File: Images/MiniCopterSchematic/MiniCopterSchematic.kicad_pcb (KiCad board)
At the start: 2 copper layers, 78.6 x 58.6 mm, 42 parts, among them J1 MPU6050, M1 Motor_DC_1, M2 Motor_DC_2, M3 Motor_DC_3, M4 Motor_DC_4, Q1 FQP20NO6L, Q2 FQP20NO6L, Q3 FQP20NO6L, Q4 FQP20NO6L

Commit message: Working on routing
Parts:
- moved Q3 13.1 mm to (92.0, 113.6)
- moved Q1 12.7 mm to (79.4, 119.0)
- moved Q4 6.32 mm to (79.3, 113.6)
- moved Q2 0.99 mm to (92.0, 119.0)
- moved kibuzzard-6440EF4B 0.98 mm to (81.6, 110.2)
- moved kibuzzard-6440D5EF 0.64 mm to (97.5, 110.6)
- moved kibuzzard-6440D61E 0.64 mm to (94.5, 109.6)
- moved kibuzzard-6440D635 0.64 mm to (91.5, 109.6)
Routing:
- net +BATT: track 0.00 -> 155.6 mm
- net Net-(Q2-Pad1): track 0.00 -> 68.1 mm
- net MOTOR_1: track 5.52 -> 56.7 mm, vias 0 -> 6
- net Net-(Q3-Pad1): track 0.00 -> 48.5 mm
- net +3V3: track 0.00 -> 29.6 mm, vias 0 -> 2
- net MOTOR_4: track 4.33 -> 30.7 mm
- net Net-(M1-Pad2): track 0.00 -> 23.9 mm
- net MOTOR_2: track 4.30 -> 24.1 mm, vias 0 -> 2
- net MOTOR_3: track 7.87 -> 21.4 mm
- net Net-(Q4-Pad1): track 0.00 -> 9.59 mm
- net SDA: track 30.3 -> 29.6 mm

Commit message: Working on PCB
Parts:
- added kibuzzard-64457E06: G***, kibuzzard-64457E06, F.Cu at (92.0, 127.0)
- added kibuzzard-64457F3E: G***, kibuzzard-64457F3E, B.Cu at (131.0, 95.0)
- moved M4 4.00 mm to (78.0, 97.0)
- moved kibuzzard-6440B803 4.00 mm to (78.0, 104.0)
- moved kibuzzard-6440B80B 4.00 mm to (78.0, 90.0)
- moved M3 1.00 mm to (101.0, 80.0)
- moved kibuzzard-6440EF4B 0.50 mm to (81.6, 110.7)
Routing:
- net Net-(M4-Pad2): track 9.59 -> 13.6 mm
- net +BATT: track 155.6 -> 157.7 mm
- net Net-(M2-Pad2): track 68.1 -> 69.7 mm
- net Net-(M3-Pad2): track 48.5 -> 47.4 mm

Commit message: Working on PCB
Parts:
- removed kibuzzard-64457E06: G***, kibuzzard-64457E06
- added kibuzzard-6445EE46: G***, kibuzzard-6445EE46, F.Cu at (92.0, 127.0)

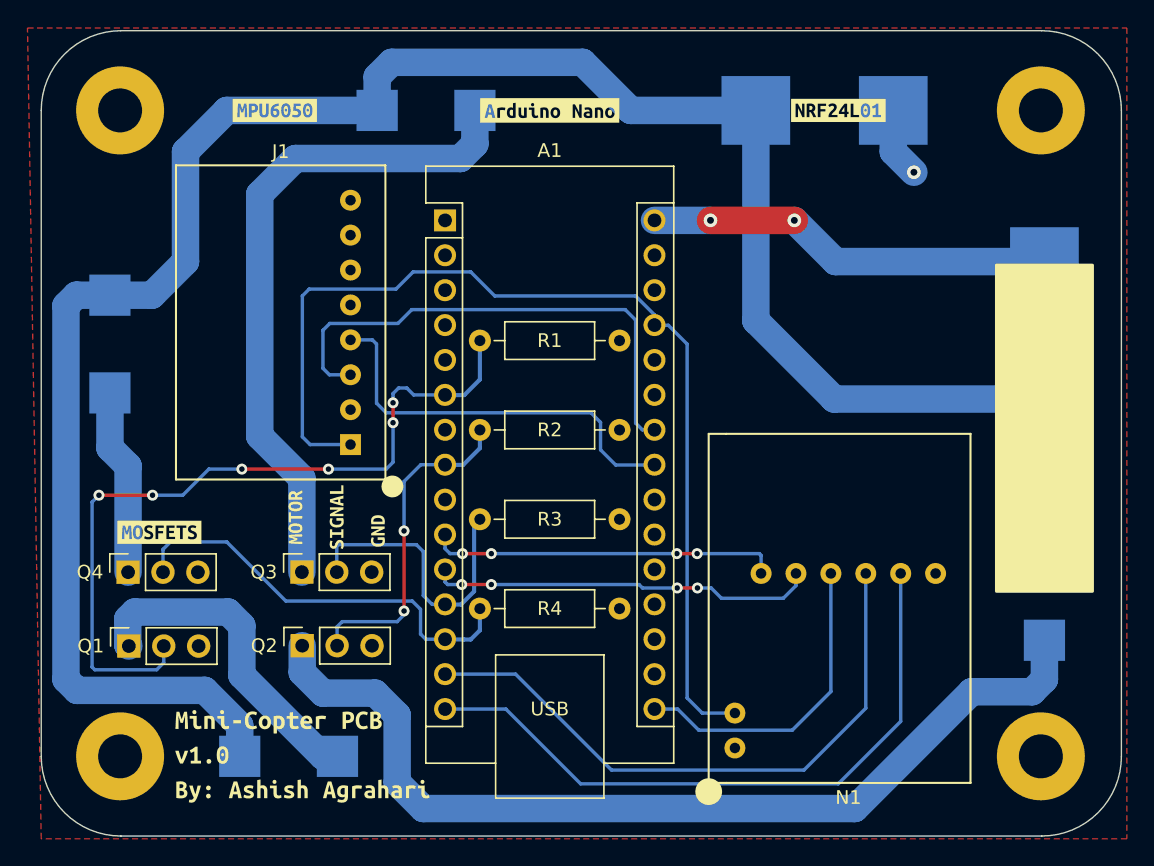
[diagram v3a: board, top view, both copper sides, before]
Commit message: Cleaning up board
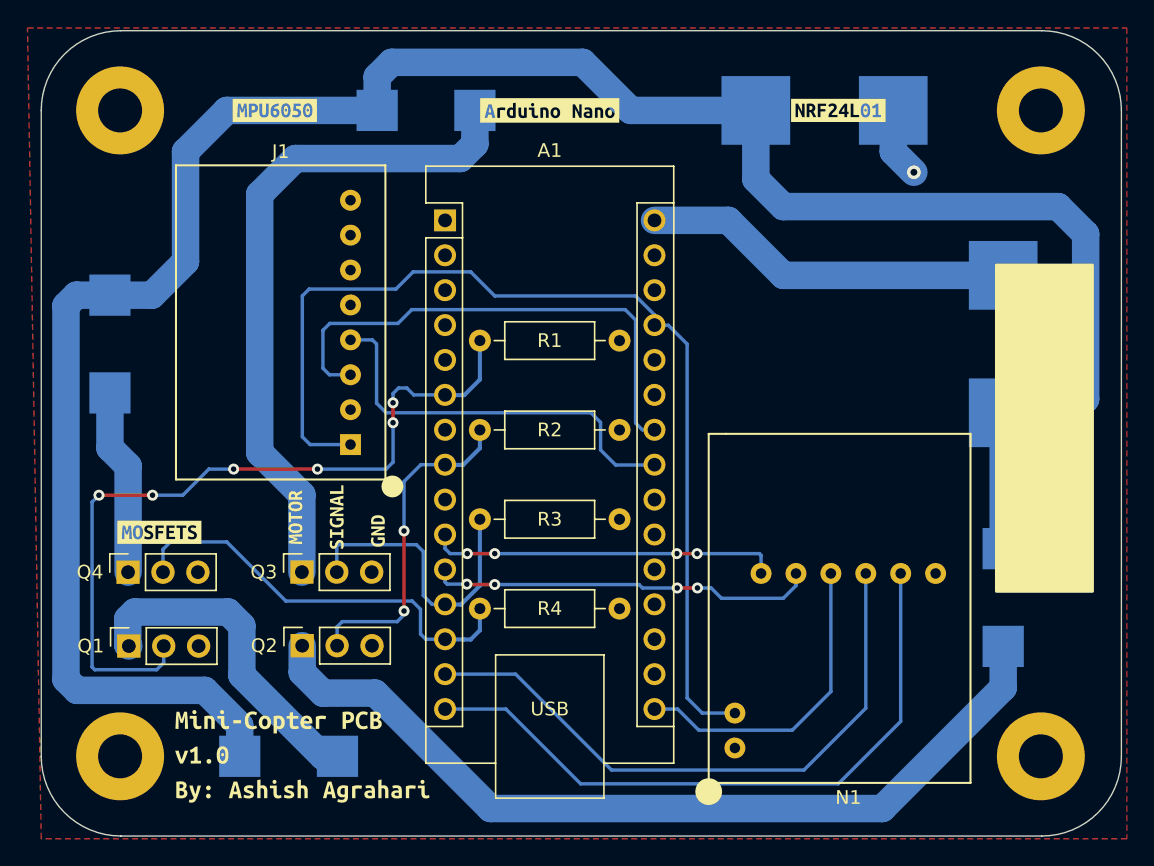
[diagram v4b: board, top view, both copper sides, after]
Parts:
- moved kibuzzard-64457F3E 5.00 mm to (126.0, 95.0)
- moved kibuzzard-6440BA11 3.61 mm to (138.0, 98.0)
- moved kibuzzard-6440B80B 3.19 mm to (143.0, 109.0)
- moved L1 3.16 mm to (143.0, 97.0)
- moved kibuzzard-6440B803 3.16 mm to (143.0, 106.0)
- moved kibuzzard-6440B80B 3.04 mm to (143.0, 87.0)
- moved M2 3.03 mm to (143.0, 115.4)
- moved kibuzzard-6440B803 3.00 mm to (143.0, 122.0)
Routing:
- net +BATT: track 157.7 -> 167.5 mm
- net Net-(M2-Pad2): track 69.7 -> 63.7 mm
- net +3V3: track 29.6 -> 27.0 mm, vias 2 -> 0

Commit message: Working on PCB
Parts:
- added C1: 47UF-CAPACITOR, Capacitor_THT:CP_Radial_D4.0mm_P1.50mm, F.Cu at (147.5, 119.0)
- added JP1: SolderJumper_1, Connector_PinSocket_2.54mm:PinSocket_1x02_P2.54mm_Vertical, F.Cu at (136.5, 77.0)
- added JP2: SolderJumper_2, Connector_PinSocket_2.54mm:PinSocket_1x02_P2.54mm_Vertical, F.Cu at (75.3, 86.5)
- moved L2 6.50 mm to (123.5, 80.0)
- moved kibuzzard-6440B80B 6.50 mm to (114.0, 80.0)
- moved kibuzzard-6440BA02 6.50 mm to (123.5, 85.0)
- moved kibuzzard-6440B803 6.00 mm to (133.5, 80.0)
- moved kibuzzard-6440B80B 2.00 mm to (78.0, 92.0)
- moved M4 1.94 mm to (78.0, 98.9)
- moved kibuzzard-6440B803 1.50 mm to (78.0, 105.5)
- moved kibuzzard-6440B80B 1.00 mm to (94.0, 80.0)
- moved kibuzzard-6440B803 0.98 mm to (108.0, 80.0)
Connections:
- A1 pad 5: unconnected-(A1-Pad5) -> INT
- J1 pad 7: unconnected-(J1-Pad7) -> Net-(J1-Pad7)
- J1 pad 8: unconnected-(J1-Pad8) -> Net-(J1-Pad8)
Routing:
- net Net-(J1-Pad7): track 0.00 -> 49.5 mm, vias 0 -> 2
- net INT: track 0.00 -> 34.7 mm, vias 0 -> 4
- net Net-(J1-Pad8): track 0.00 -> 20.2 mm, vias 0 -> 2
- net Net-(M4-Pad2): track 13.6 -> 11.6 mm
- net +BATT: track 167.5 -> 165.8 mm
- net GND: track 5.12 -> 6.83 mm
- net Net-(M3-Pad2): track 47.4 -> 48.0 mm

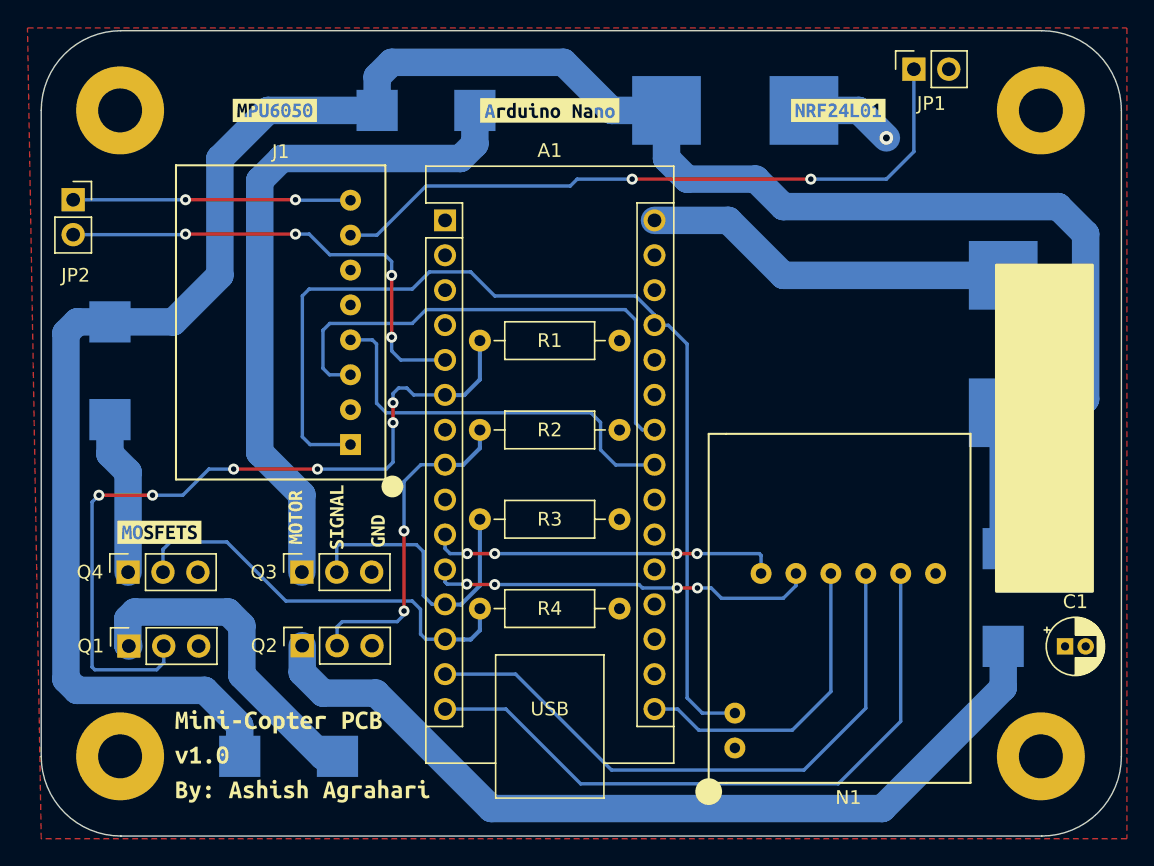
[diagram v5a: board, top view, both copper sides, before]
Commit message: Added capacitor, changed track widths on PCB
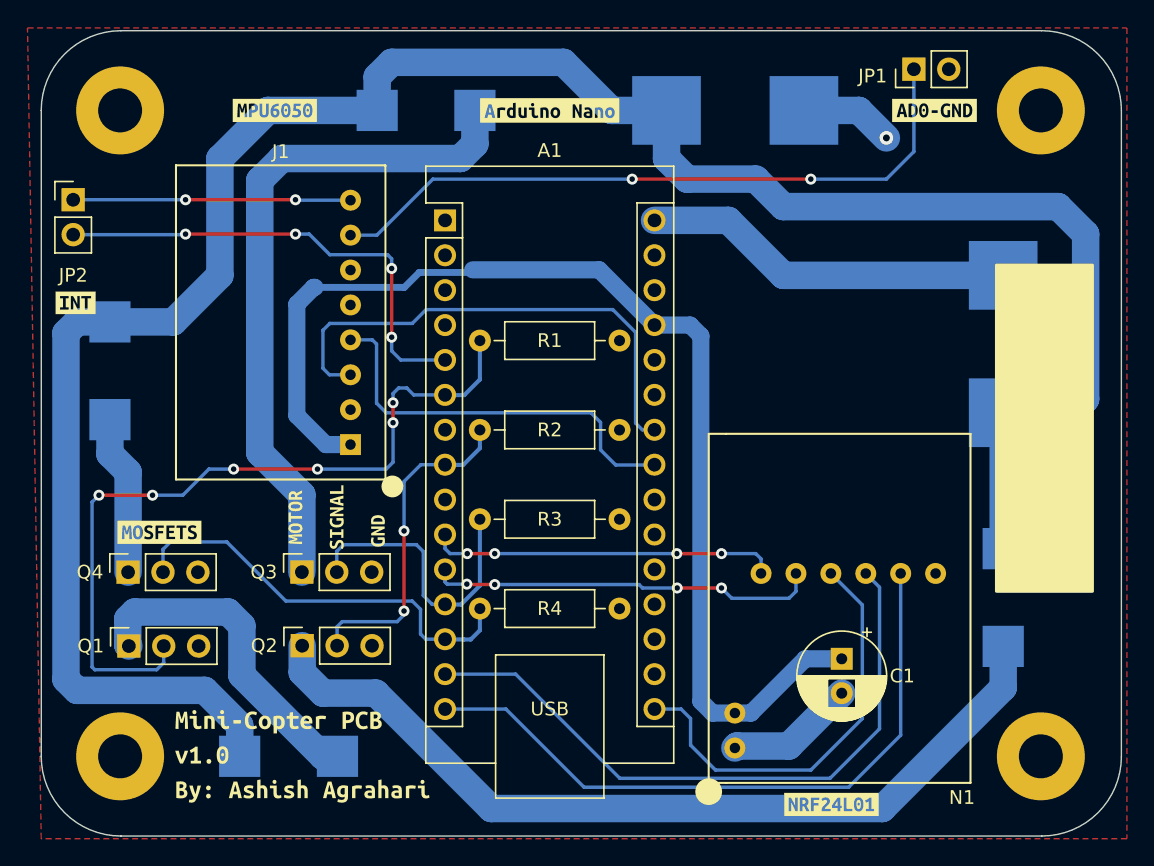
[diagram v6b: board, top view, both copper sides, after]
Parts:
- added kibuzzard-644B0C07: G***, kibuzzard-644B0C07, F.Cu at (138.0, 80.0)
- added kibuzzard-644B0C24: G***, kibuzzard-644B0C24, F.Cu at (75.5, 94.0)
- C1: footprint Capacitor_THT:CP_Radial_D4.0mm_P1.50mm -> Capacitor_THT:CP_Radial_D6.3mm_P2.50mm
- JP1, JP2: footprint Connector_PinSocket_2.54mm:PinSocket_1x02_P2.54mm_Vertical -> Connector_PinHeader_2.54mm:PinHeader_1x02_P2.54mm_Vertical
- moved kibuzzard-6440AFCF 50.5 mm to (130.5, 130.5)
- moved C1 16.3 mm to (131.2, 119.9), turned to -90 degrees
- moved kibuzzard-64457F3E 2.00 mm to (128.0, 95.0)
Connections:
- C1 pad 1: (no net) -> +5V
- C1 pad 2: (no net) -> GND
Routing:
- net GND: track 6.83 -> 16.3 mm
- net +5V: track 74.9 -> 84.1 mm
- net SCK_NANO: track 23.2 -> 31.2 mm
- net MOSI_NANO: track 45.2 -> 48.0 mm
- net MISO_NANO: track 48.1 -> 48.8 mm
- net SCL: track 37.7 -> 37.2 mm

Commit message: Added LEDs
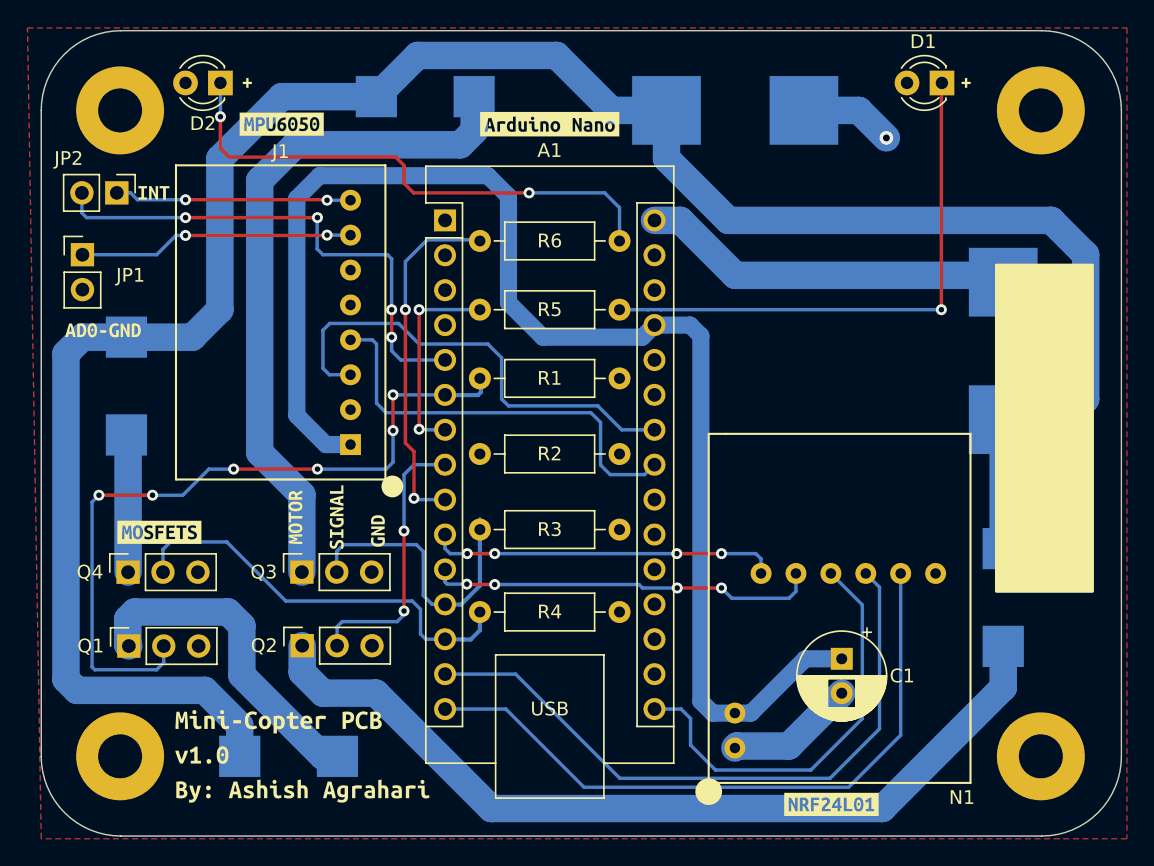
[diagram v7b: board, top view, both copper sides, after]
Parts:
- removed kibuzzard-644B0C07: G***, kibuzzard-644B0C07
- removed kibuzzard-644B0C24: G***, kibuzzard-644B0C24
- added D1: LED_3MM, LED_THT:LED_D3.0mm, F.Cu at (138.5, 78.0)
- added D2: LED_3MM, LED_THT:LED_D3.0mm, F.Cu at (86.0, 78.0)
- added R5: 100 Ω, Resistor_THT:R_Axial_DIN0207_L6.3mm_D2.5mm_P10.16mm_Horizontal, F.Cu at (104.9, 94.5)
- added R6: 100 Ω, Resistor_THT:R_Axial_DIN0207_L6.3mm_D2.5mm_P10.16mm_Horizontal, F.Cu at (104.9, 89.5)
- added kibuzzard-644C41F3: G***, kibuzzard-644C41F3, F.Cu at (81.2, 86.0)
- added kibuzzard-644C4204: G***, kibuzzard-644C4204, F.Cu at (77.5, 96.0)
- added kibuzzard-644C468F: G***, kibuzzard-644C468F, F.Cu at (88.0, 78.0)
- added kibuzzard-644C469B: G***, kibuzzard-644C469B, F.Cu at (140.3, 78.0)
- moved JP1 62.0 mm to (76.0, 90.5), turned to 0 degrees
- moved JP2 3.21 mm to (78.5, 86.0), turned to -90 degrees
- moved R1 2.75 mm to (104.9, 99.5)
- moved kibuzzard-6440B803 1.80 mm to (79.0, 107.0)
- moved R2 1.75 mm to (104.9, 105.0)
- moved M4 1.64 mm to (79.2, 100.1)
- moved kibuzzard-6440B80B 1.43 mm to (79.0, 93.0)
- moved kibuzzard-6440AF37 1.12 mm to (90.5, 81.0)
- moved M3 1.00 mm to (100.9, 79.0)
- moved kibuzzard-6440AFC4 1.00 mm to (110.0, 81.0)
- moved kibuzzard-6440B803 1.00 mm to (108.0, 79.0)
- moved kibuzzard-6440B80B 1.00 mm to (94.0, 79.0)
- moved kibuzzard-6440B80B 1.00 mm to (143.0, 88.0)
- moved R3 0.75 mm to (104.9, 110.5)
- moved L1 0.50 mm to (143.0, 97.5)
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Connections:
- A1 pad 7: unconnected-(A1-Pad7) -> LED_1
- A1 pad 9: unconnected-(A1-Pad9) -> LED_2
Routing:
- net Net-(D1-Pad1): track 0.00 -> 39.9 mm, vias 0 -> 1
- net Net-(D2-Pad1): track 0.00 -> 38.8 mm, vias 0 -> 2
- net Net-(J1-Pad7): track 49.5 -> 20.1 mm
- net LED_2: track 0.00 -> 25.9 mm, vias 0 -> 2
- net +5V: track 84.1 -> 99.6 mm
- net LED_1: track 0.00 -> 15.0 mm, vias 0 -> 2
- net MOTOR_2: track 24.1 -> 20.1 mm
- net Net-(J1-Pad8): track 20.2 -> 17.2 mm
- net SCL: track 37.2 -> 34.3 mm
- net INT: track 34.8 -> 37.6 mm
- net MOTOR_1: track 56.5 -> 54.2 mm
- net Net-(M4-Pad2): track 11.6 -> 10.0 mm
- net Net-(M3-Pad2): track 48.0 -> 49.4 mm
- net +BATT: track 165.8 -> 164.5 mm
- net SDA: track 29.6 -> 30.8 mm

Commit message: Making PCB look good
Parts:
- removed kibuzzard-6445EE46: G***, kibuzzard-6445EE46
- removed kibuzzard-644C41F3: G***, kibuzzard-644C41F3
- removed kibuzzard-644C4204: G***, kibuzzard-644C4204
- added kibuzzard-644C8A62: G***, kibuzzard-644C8A62, F.Cu at (92.0, 127.0)
- moved JP1 2.20 mm to (78.1, 90.0), turned to -90 degrees
- moved D1 1.16 mm to (139.7, 78.0)
- moved kibuzzard-644C469B 1.16 mm to (141.5, 78.0)
- moved kibuzzard-6440AF37 0.91 mm to (90.6, 81.9)
- moved kibuzzard-6440AFC4 0.89 mm to (109.6, 81.8)
- moved kibuzzard-64457F3E 0.73 mm to (128.2, 95.7)
- moved JP2 0.36 mm to (78.1, 86.0)
- moved R5 0.10 mm to (104.9, 94.4)
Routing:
- net GND: track 16.3 -> 12.9 mm
- net MOTOR_2: track 20.1 -> 23.0 mm
- net Net-(J1-Pad7): track 20.1 -> 17.7 mm, vias 2 -> 1
- net +BATT: track 164.5 -> 165.7 mm
- net Net-(D2-Pad1): track 38.8 -> 38.0 mm, vias 2 -> 1
- net Net-(D1-Pad1): track 39.9 -> 39.3 mm, vias 1 -> 2
- net LED_1: track 15.0 -> 14.6 mm, vias 2 -> 1
- net Net-(J1-Pad8): track 17.2 -> 17.6 mm, vias 2 -> 1
- net LED_2: track 25.9 -> 25.7 mm, vias 2 -> 1
